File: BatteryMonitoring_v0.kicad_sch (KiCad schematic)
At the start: 32 parts, among them J5 Conn_02x08_Odd_Even, J7 Conn_01x03_Pin, Q6 NPN, SW3 RST_SHUT, SW4 WAKE, U2 PBQ76952PFBT

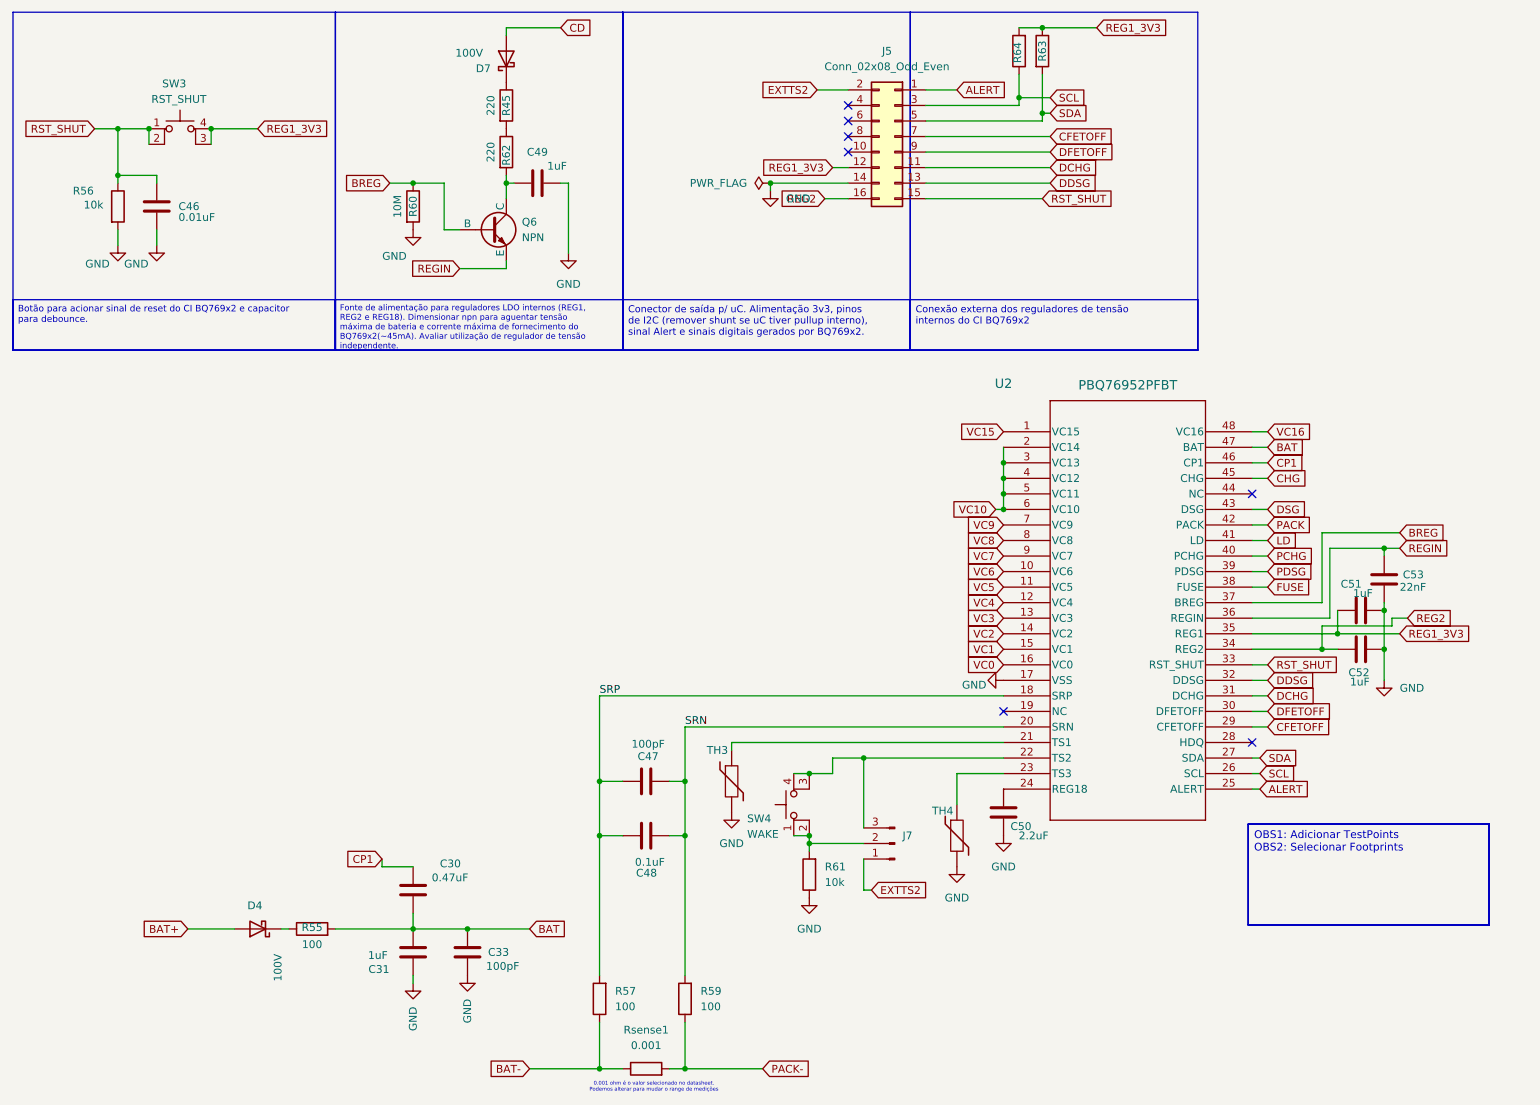
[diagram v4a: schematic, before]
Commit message: posiciona testpoints
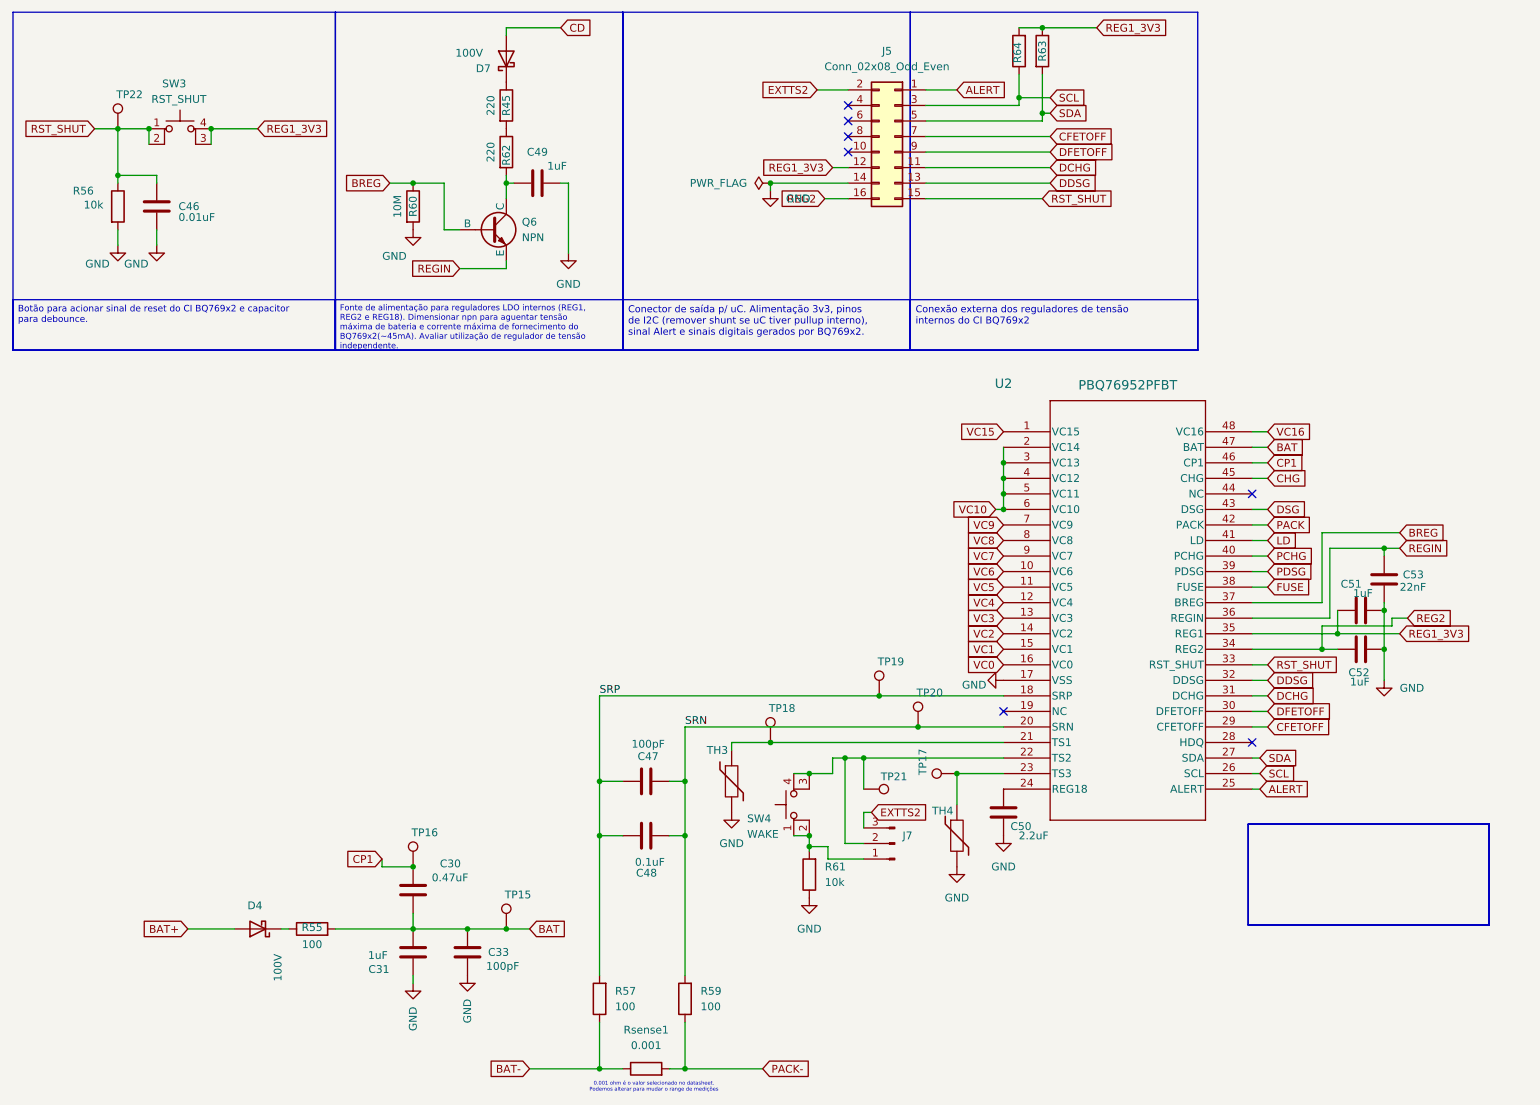
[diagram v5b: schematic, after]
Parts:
- added TP15, TP16, TP17, TP18, TP19, TP20, TP21, TP22: TestPoint, TestPoint:TestPoint_Loop_D3.80mm_Drill2.5mm, symbol Connector:TestPoint
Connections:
- net BAT: now also TP15.1
- net CP1: now also TP16.1
- net EXTTS2: now also J7.3 (Pin_3); no longer J7.1 (Pin_1)
- net RST_SHUT: now also TP22.1
- net SRN: now also TP20.1
- net SRP: now also TP19.1
- net at TH3.1, U2.21 (TS1): now also TP18.1
- net at SW4.3 (K), SW4.4 (A), U2.22 (TS2): now also J7.2 (Pin_2), TP21.1; no longer J7.3 (Pin_3)
- net at TH4.1, U2.23 (TS3): now also TP17.1
- net at R61.2, SW4.1, SW4.2: now also J7.1 (Pin_1); no longer J7.2 (Pin_2)
